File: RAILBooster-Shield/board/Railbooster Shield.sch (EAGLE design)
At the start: 39 parts, among them IC1 LMD18200, IC2 LM358D, IC3 V_REG_LD1085D2, IC4 IC_555-SOIC8, J1 POWER_JACKPTH, U1 ARDUINOR3-DIMENSION, X4 SCREWTERMINAL-5.08-2

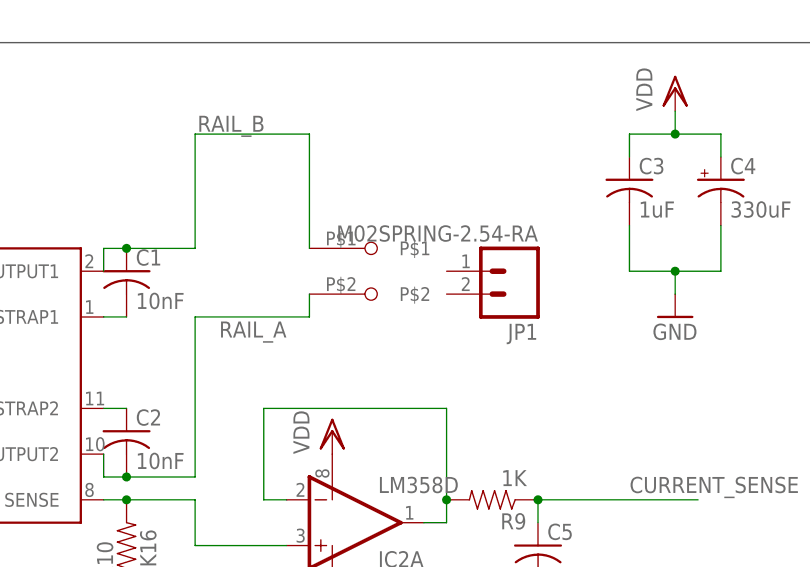
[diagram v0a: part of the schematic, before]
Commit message: Update to remove rouge connector
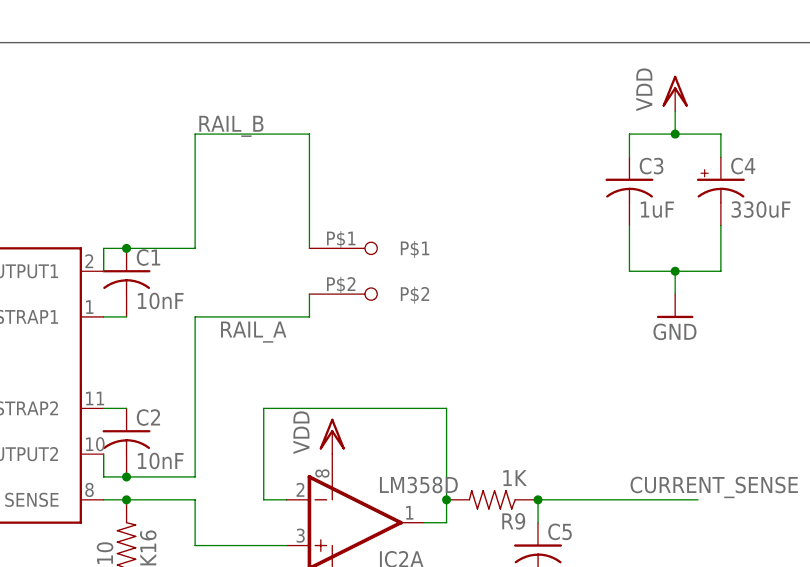
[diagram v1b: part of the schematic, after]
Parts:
- removed JP1: M02SPRING-2.54-RA, SparkFun-Connectors:M02SPRING-2.54-RA
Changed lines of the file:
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@@
 <part name="C10" library="resistor" deviceset="C-US" device="C1206" value="10uF"/>
 <part name="GND13" library="supply1" deviceset="GND" device=""/>
-<part name="JP1" library="SparkFun-Connectors" deviceset="M02" device="SPRING-2.54-RA"/>
 </parts>
 <sheets>
@@
 <instance part="C10" gate="G$1" x="332.74" y="78.74"/>
 <instance part="GND13" gate="1" x="332.74" y="68.58"/>
-<instance part="JP1" gate="G$1" x="236.22" y="154.94" rot="R180"/>
 </instances>
 <busses>
